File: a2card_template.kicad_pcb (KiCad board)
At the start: 2 copper layers, 158.8 x 76.4 mm, 10 parts, among them U10 PLCCZ80, U14 74LS367, U15 74LS373, U16 74LS367, U17 74LS367, U9 74LS367

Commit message: Cleaning up footprints
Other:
- board text added: "TODO: Pin numbers seem wrong - is connector flipped?"
- board text removed: "26"
- board text removed: "50"
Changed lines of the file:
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@@
   (general
     (thickness 1.6)
-    (drawings 50)
+    (drawings 49)
     (tracks 4)
     (zones 0)
@@
       (effects (font (size 1 1) (thickness 0.15)))
     )
-    (fp_text value 74LS367 (at 3.81 20.11) (layer F.Fab)
+    (fp_text value 74LS367 (at 3.81 20.11) (layer F.SilkS)
       (effects (font (size 1 1) (thickness 0.15)))
     )
@@
       (effects (font (size 1 1) (thickness 0.15)))
     )
-    (fp_text value 10kΩ (at 11.43 2.4) (layer F.Fab)
+    (fp_text value 10kΩ (at 11.43 2.4) (layer F.SilkS)
       (effects (font (size 1 1) (thickness 0.15)))
     )
@@
       (effects (font (size 1 1) (thickness 0.15)))
     )
-    (fp_text value 10kΩ (at 6.35 2.4) (layer F.Fab)
+    (fp_text value 10kΩ (at 6.35 2.4) (layer F.SilkS)
       (effects (font (size 1 1) (thickness 0.15)))
     )
@@
       (net 17 "Net-(BUS1-Pad1)"))
   )
-  (gr_text 50 (at 153.67 123.698) (layer F.SilkS)
+  (gr_text "TODO: Pin numbers seem wrong - is connector flipped?" (at 168.91 135.89) (layer Dwgs.User)
     (effects (font (size 1 1) (thickness 0.15)))
   )
-  (gr_text 26 (at 217.932 123.952) (layer F.SilkS)
-    (effects (font (size 1 1) (thickness 0.15)))
-  )

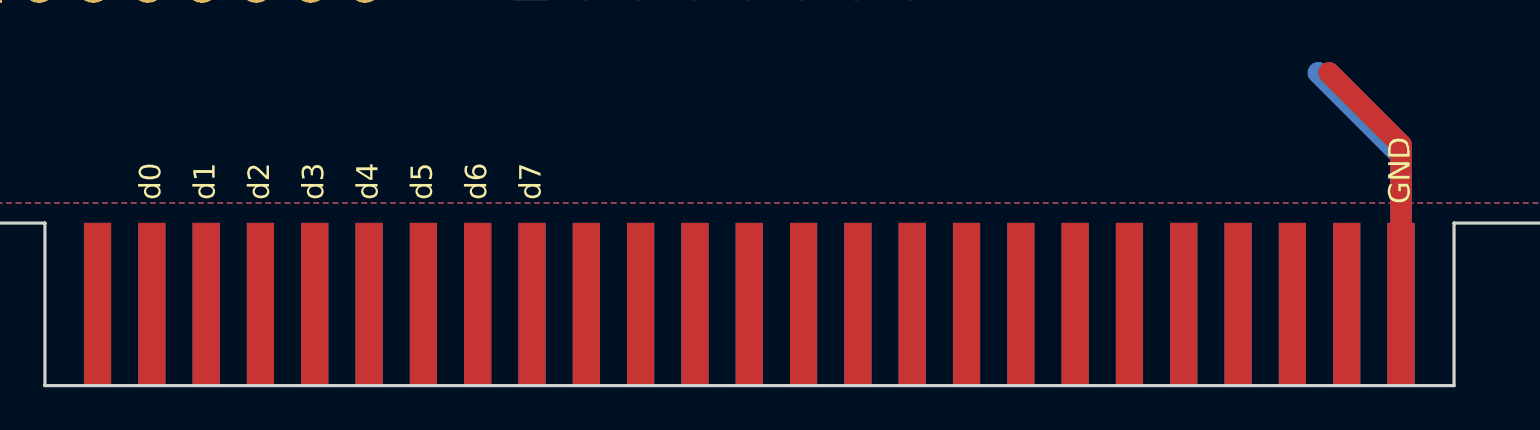
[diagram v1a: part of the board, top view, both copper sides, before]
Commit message: Flip the connector so 1-25 are on the front
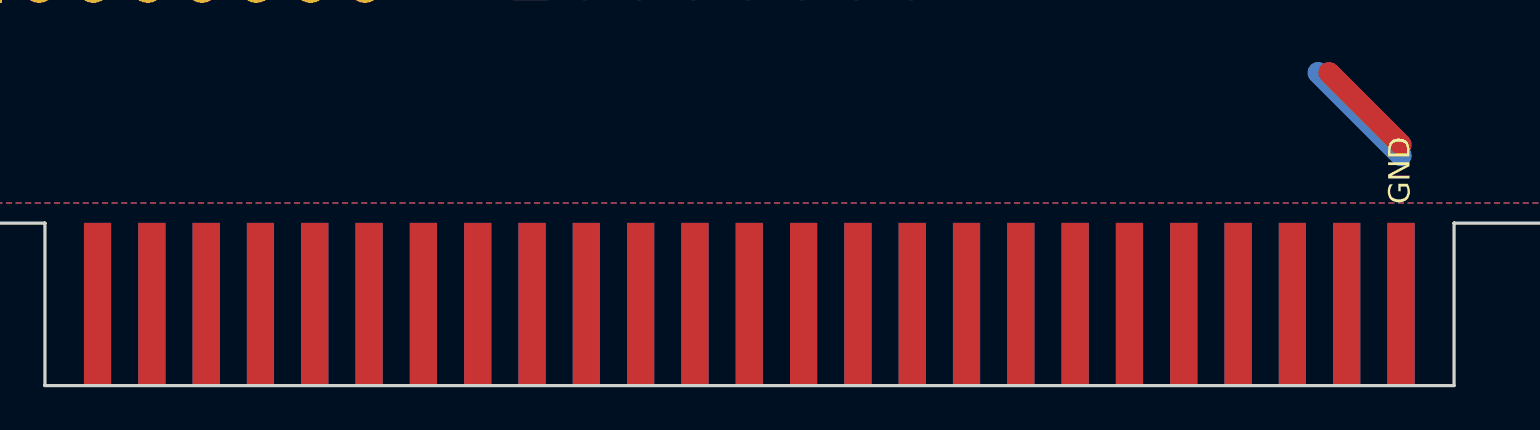
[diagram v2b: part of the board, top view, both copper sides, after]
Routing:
- net +5V: track 12.4 -> 4.76 mm
- net GND: track 12.2 -> 5.48 mm
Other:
- board text removed: "TODO: Pin numbers seem wrong - is connector flipped?"
- board text removed: "a0"
- board text removed: "a1"
- board text removed: "a10"
- board text removed: "a11"
- board text removed: "a12"
- board text removed: "a13"
- board text removed: "a14"
- board text removed: "a15"
- board text removed: "a2"
- board text removed: "a3"
- board text removed: "a4"
- board text removed: "a5"
- board text removed: "a6"
- board text removed: "a7"
- board text removed: "a8"
- board text removed: "a9"
- board text removed: "d0"
- board text removed: "d1"
- board text removed: "d2"
- board text removed: "d3"
- board text removed: "d4"
- board text removed: "d5"
- board text removed: "d6"
- board text removed: "d7"

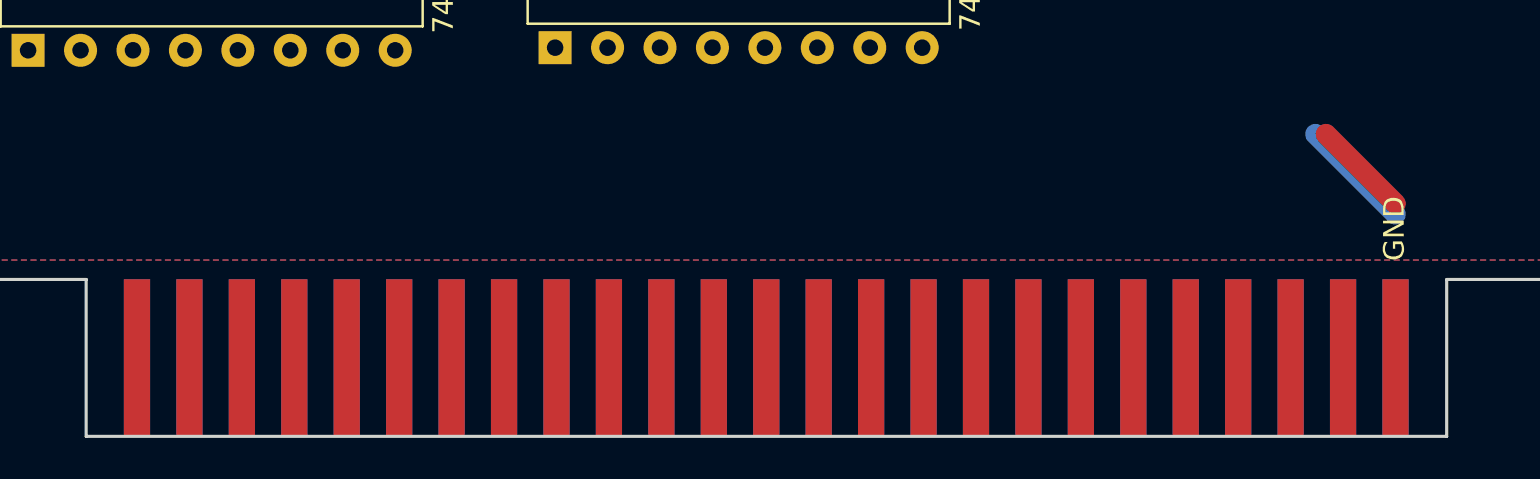
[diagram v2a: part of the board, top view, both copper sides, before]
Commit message: Move fingers up so it can be beveled
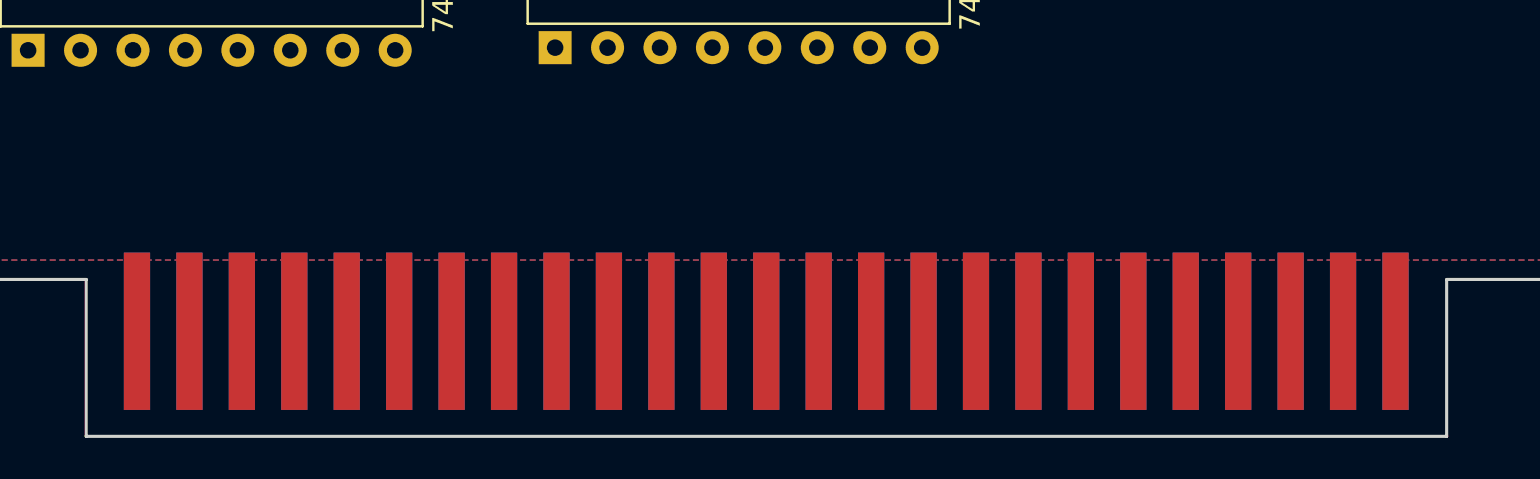
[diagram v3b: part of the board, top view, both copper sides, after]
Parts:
- moved BUS1 1.29 mm to (185.7, 124.1)
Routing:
- net GND: track 5.48 -> 0.00 mm
- net +5V: track 4.76 -> 0.00 mm
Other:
- board text removed: "+5V"
- board text removed: "GND"
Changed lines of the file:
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@@
   (general
     (thickness 1.6)
-    (drawings 25)
-    (tracks 2)
+    (drawings 23)
+    (tracks 0)
     (zones 0)
     (modules 10)
@@
   )
   (module Apple_ii_card:AppleII_card_edge (layer F.Cu)
-    (at 185.74 125.39)
+    (at 185.74 124.1)
     (fp_text reference BUS1 (at -30.48 -1.27) (layer F.SilkS) hide
       (effects (font (size 1 1) (thickness 0.15)))
@@
     (arrow2b (pts (xy 230.0224 133) (xy 229.435979 131.873496)))
   )
-  (gr_text GND (at 216.154 122.936 90) (layer F.SilkS)
-    (effects (font (size 1 1) (thickness 0.15)))
-  )
-  (gr_text +5V (at 216.154 122.936 90) (layer B.SilkS)
-    (effects (font (size 1 1) (thickness 0.15)) (justify mirror))
-  )
   (gr_poly (pts (xy 219.456 133.604) (xy 152.4 133.604) (xy 152.4 125.984) (xy 219.456 125.984)) (layer B.Mask) (width 0.1))
   (gr_poly (pts (xy 219.456 133.604) (xy 152.4 133.604) (xy 152.4 125.984) (xy 219.456 125.984)) (layer F.Mask) (width 0.1))
@@
   (gr_line (start 69.5 56.6) (end 228.3 56.6) (layer Edge.Cuts) (width 0.15))
   (gr_line (start 69.5 125.4) (end 69.5 56.6) (layer Edge.Cuts) (width 0.15))
-  (segment (start 216.22 121.732) (end 212.852 118.364) (width 1) (layer F.Cu) (net 29))
-  (segment (start 216.22 122.24) (end 212.344 118.364) (width 1) (layer B.Cu) (net 28))
   (zone (net 28) (net_name GND) (layer F.Cu) (hatch edge 0.508)
     (connect_pads (clearance 0.508))

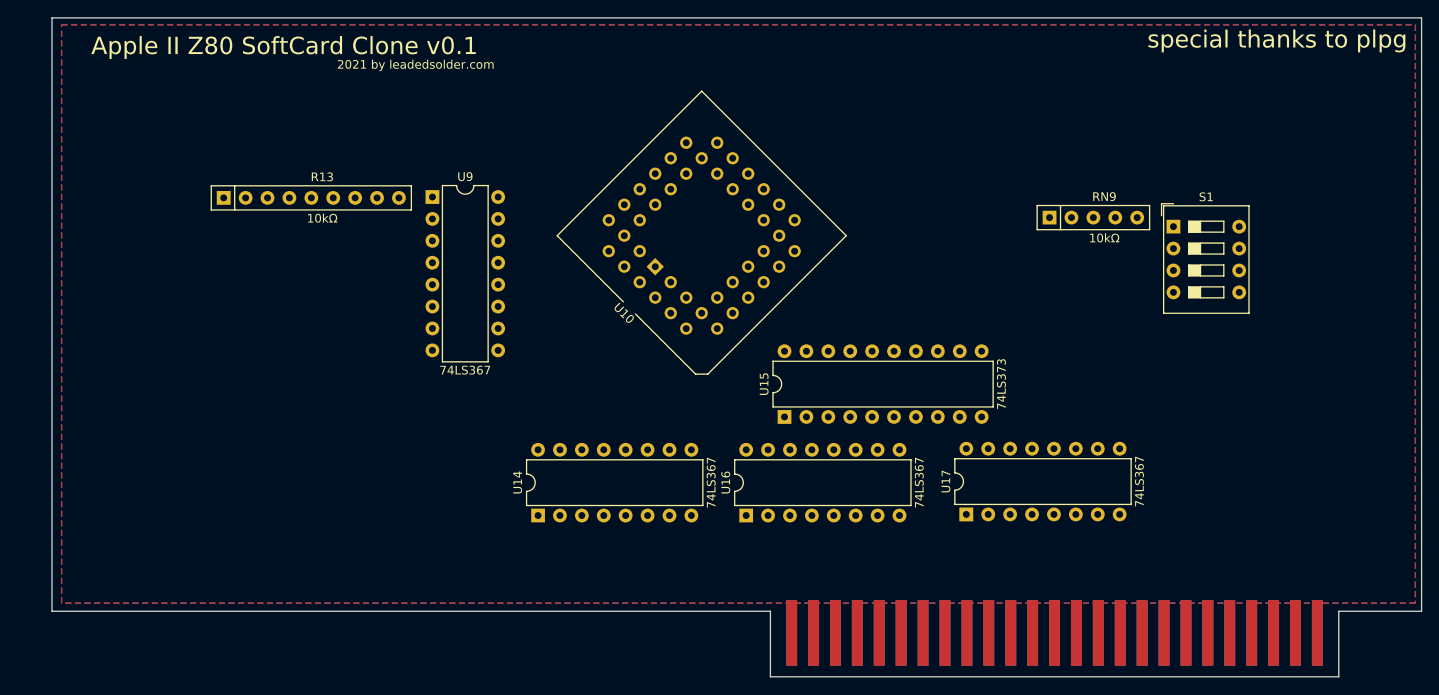
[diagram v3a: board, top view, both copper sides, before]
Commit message: Flip fills
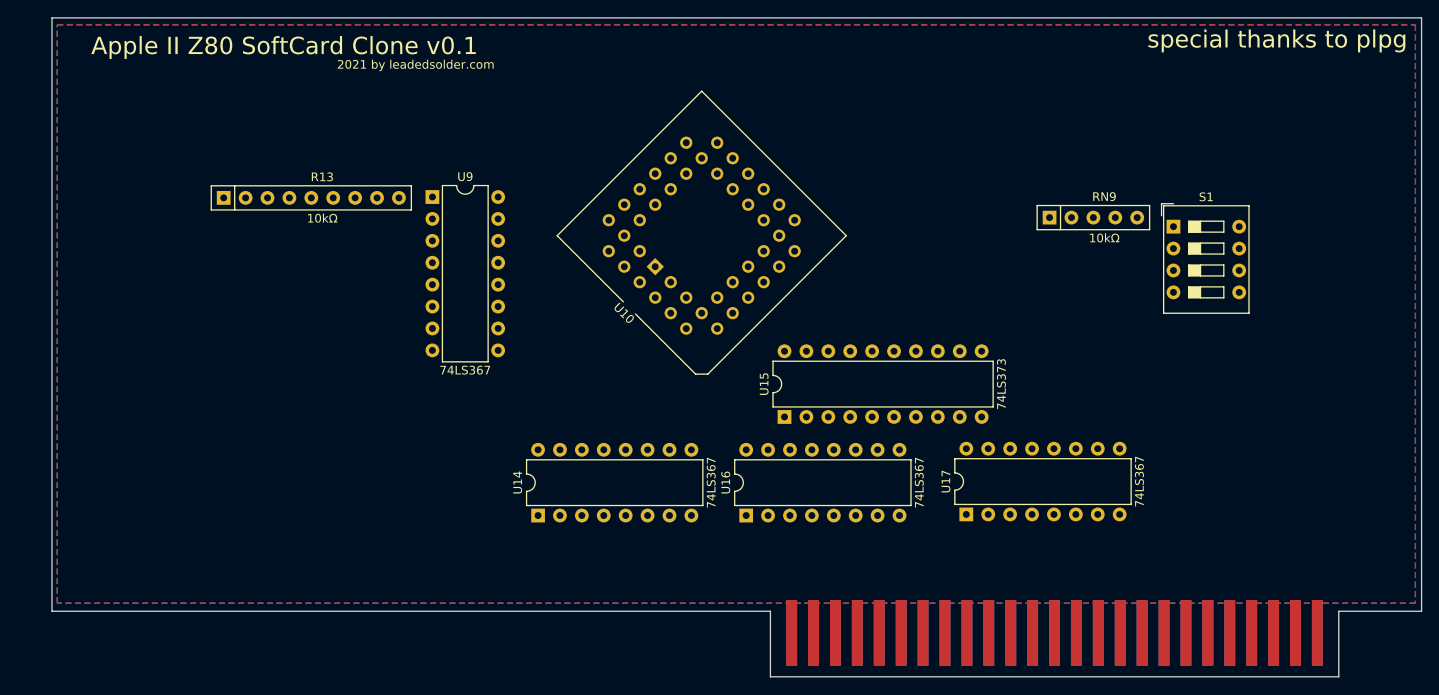
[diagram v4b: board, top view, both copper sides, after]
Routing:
- added copper zone on F.Cu, net +5V
- added copper zone on B.Cu, net GND
- removed copper zone on B.Cu, net +5V
- removed copper zone on F.Cu, net GND
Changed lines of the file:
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@@
   (gr_line (start 69.5 56.6) (end 228.3 56.6) (layer Edge.Cuts) (width 0.15))
   (gr_line (start 69.5 125.4) (end 69.5 56.6) (layer Edge.Cuts) (width 0.15))
-  (zone (net 28) (net_name GND) (layer F.Cu) (hatch edge 0.508)
+  (zone (net 29) (net_name +5V) (layer F.Cu) (hatch edge 0.508)
     (connect_pads (clearance 0.508))
     (min_thickness 0.254)
@@
     (polygon
       (pts
-        (xy 227.584 124.46) (xy 70.612 124.46) (xy 70.612 57.404) (xy 227.584 57.404)
+        (xy 227.584 124.46) (xy 70.104 124.46) (xy 70.104 57.404) (xy 227.584 57.404)
       )
     )
   )
-  (zone (net 29) (net_name +5V) (layer B.Cu) (hatch edge 0.508)
+  (zone (net 28) (net_name GND) (layer B.Cu) (hatch edge 0.508)
     (connect_pads (clearance 0.508))
     (min_thickness 0.254)
@@
     (polygon
       (pts
-        (xy 227.584 124.46) (xy 70.612 124.46) (xy 70.612 57.404) (xy 227.584 57.404)
+        (xy 227.584 124.46) (xy 70.104 124.46) (xy 70.104 57.404) (xy 227.584 57.404)
       )
     )

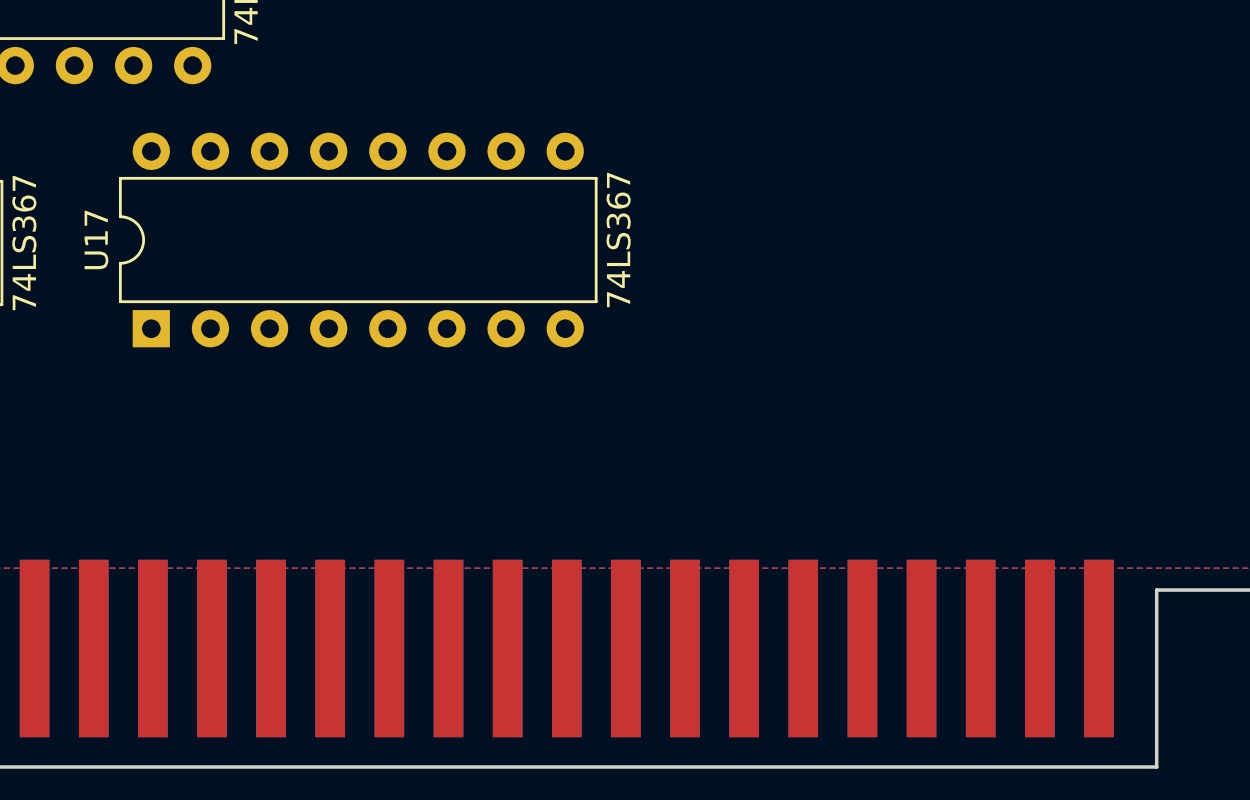
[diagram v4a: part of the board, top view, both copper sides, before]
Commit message: More fill cleanup
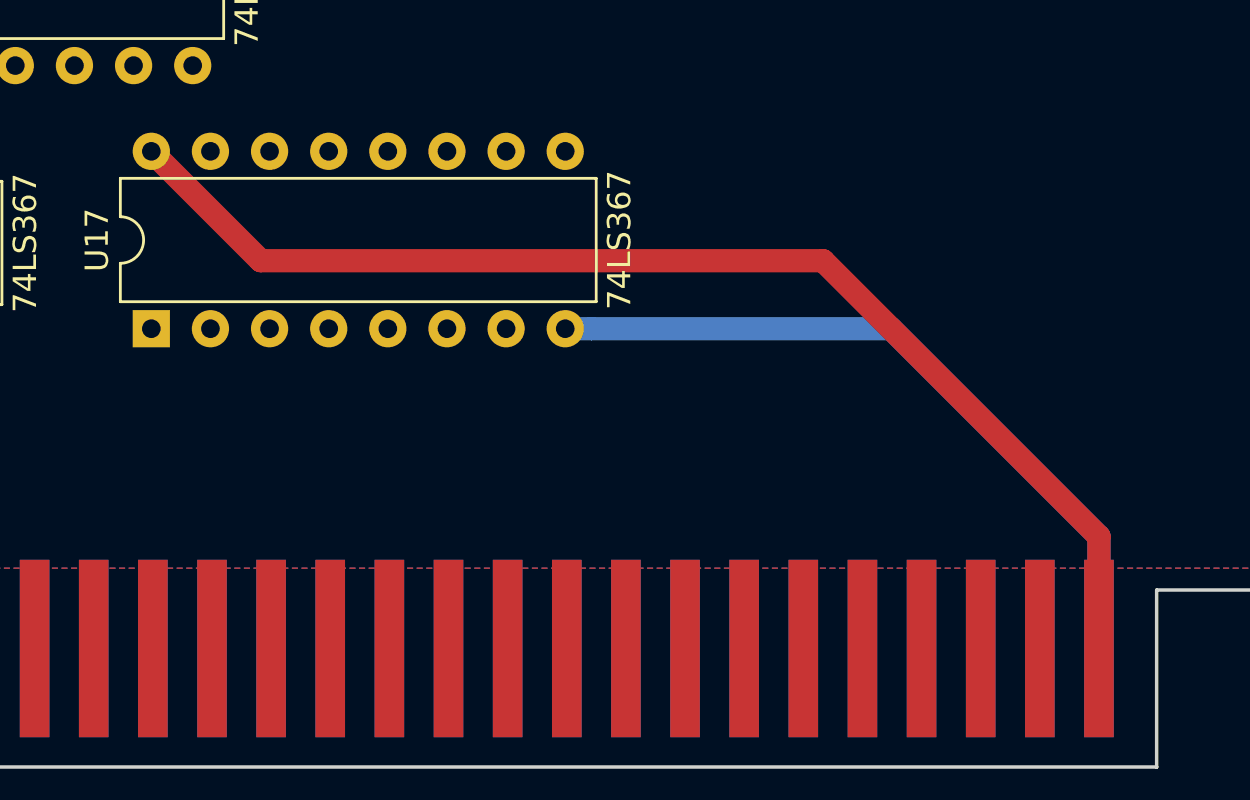
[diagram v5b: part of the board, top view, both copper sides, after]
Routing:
- net +5V: track 0.00 -> 52.4 mm
- net GND: track 0.00 -> 31.4 mm
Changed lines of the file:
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@@
     (thickness 1.6)
     (drawings 23)
-    (tracks 0)
+    (tracks 8)
     (zones 0)
     (modules 10)
@@
   )
   (setup
-    (last_trace_width 0.25)
+    (last_trace_width 1)
     (user_trace_width 0.5)
     (user_trace_width 1)
@@
   (gr_line (start 69.5 56.6) (end 228.3 56.6) (layer Edge.Cuts) (width 0.15))
   (gr_line (start 69.5 125.4) (end 69.5 56.6) (layer Edge.Cuts) (width 0.15))
+  (segment (start 207.293 114.173) (end 194.42537 114.173) (width 1) (layer B.Cu) (net 28))
+  (segment (start 194.42537 114.173) (end 193.294 114.173) (width 1) (layer B.Cu) (net 28))
+  (segment (start 216.22 123.1) (end 207.293 114.173) (width 1) (layer B.Cu) (net 28))
+  (segment (start 216.22 127.91) (end 216.22 123.1) (width 1) (layer B.Cu) (net 28))
+  (segment (start 216.22 123.1) (end 204.372 111.252) (width 1) (layer F.Cu) (net 29))
+  (segment (start 216.22 127.91) (end 216.22 123.1) (width 1) (layer F.Cu) (net 29))
+  (segment (start 180.213 111.252) (end 175.514 106.553) (width 1) (layer F.Cu) (net 29))
+  (segment (start 204.372 111.252) (end 180.213 111.252) (width 1) (layer F.Cu) (net 29))
   (zone (net 29) (net_name +5V) (layer F.Cu) (hatch edge 0.508)
     (connect_pads (clearance 0.508))

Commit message: Pin numbers
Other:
- board text added: "1"
- board text added: "25"
- board text added: "26"
- board text added: "50"
- board text added: "d0"
- board text added: "d1"
- board text added: "d2"
- board text added: "d3"
- board text added: "d4"
- board text added: "d5"
- board text added: "d6"
- board text added: "d7"
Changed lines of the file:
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@@
   (general
     (thickness 1.6)
-    (drawings 23)
+    (drawings 35)
     (tracks 8)
     (zones 0)
@@
       (net 17 "Net-(BUS1-Pad1)"))
   )
+  (gr_text d7 (at 175.514 122.936 90) (layer B.SilkS)
+    (effects (font (size 1 1) (thickness 0.15)) (justify mirror))
+  )
+  (gr_text d6 (at 172.974 122.936 90) (layer B.SilkS)
+    (effects (font (size 1 1) (thickness 0.15)) (justify mirror))
+  )
+  (gr_text d5 (at 170.434 122.936 90) (layer B.SilkS)
+    (effects (font (size 1 1) (thickness 0.15)) (justify mirror))
+  )
+  (gr_text d4 (at 167.894 122.936 90) (layer B.SilkS)
+    (effects (font (size 1 1) (thickness 0.15)) (justify mirror))
+  )
+  (gr_text d3 (at 165.354 122.936 90) (layer B.SilkS)
+    (effects (font (size 1 1) (thickness 0.15)) (justify mirror))
+  )
+  (gr_text d2 (at 162.814 122.936 90) (layer B.SilkS)
+    (effects (font (size 1 1) (thickness 0.15)) (justify mirror))
+  )
+  (gr_text d1 (at 160.274 122.936 90) (layer B.SilkS)
+    (effects (font (size 1 1) (thickness 0.15)) (justify mirror))
+  )
+  (gr_text d0 (at 157.734 122.936 90) (layer B.SilkS)
+    (effects (font (size 1 1) (thickness 0.15)) (justify mirror))
+  )
+  (gr_text 50 (at 153.416 123.444) (layer B.SilkS)
+    (effects (font (size 1 1) (thickness 0.15)) (justify mirror))
+  )
+  (gr_text 26 (at 218.44 123.444) (layer B.SilkS)
+    (effects (font (size 1 1) (thickness 0.15)) (justify mirror))
+  )
+  (gr_text 25 (at 218.44 123.444) (layer F.SilkS)
+    (effects (font (size 1 1) (thickness 0.15)))
+  )
+  (gr_text 1 (at 153.416 123.444) (layer F.SilkS)
+    (effects (font (size 1 1) (thickness 0.15)))
+  )
   (dimension 1.174 (width 0.15) (layer Cmts.User)
